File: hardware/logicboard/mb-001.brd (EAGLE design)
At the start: 91 x 57 mm, 11 parts, among them J7 DIN5, J8 DIN5, J9 DIN5

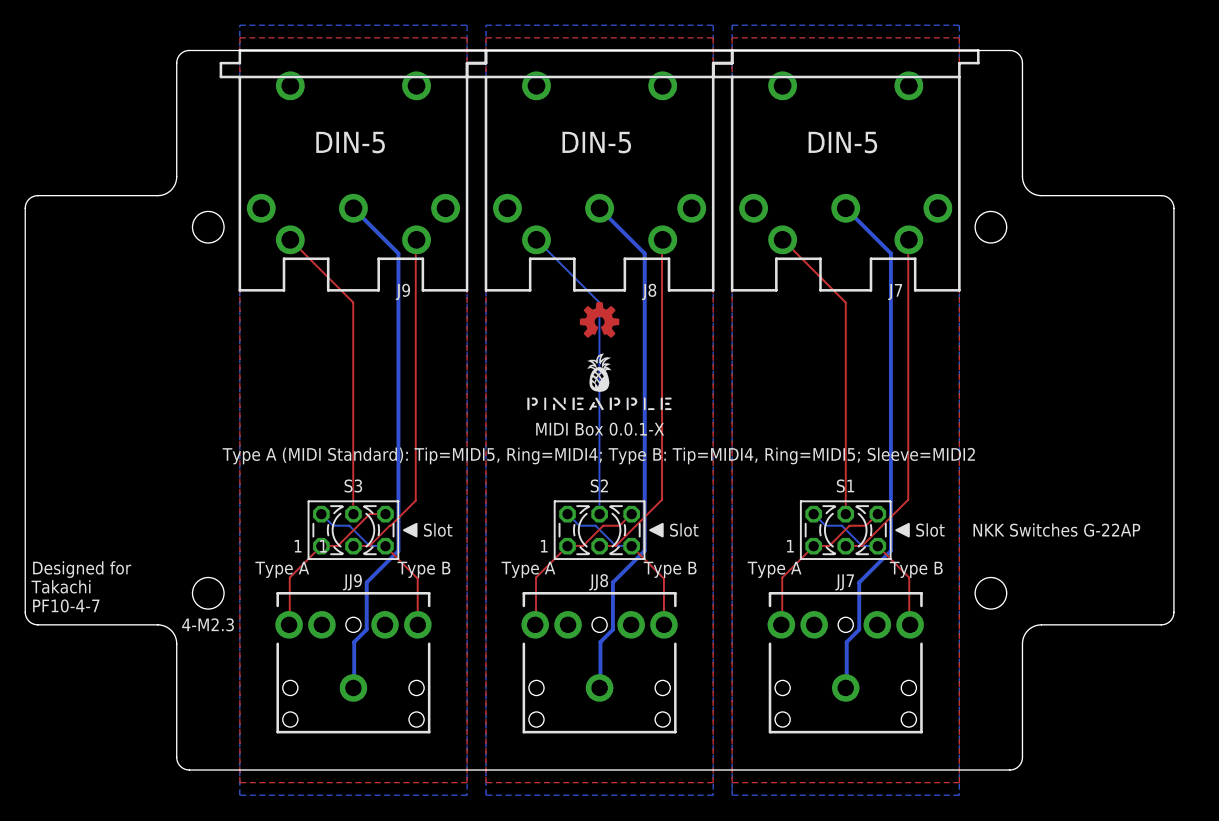
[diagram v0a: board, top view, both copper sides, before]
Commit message: Fixed silk and signal names. No pattern changed.
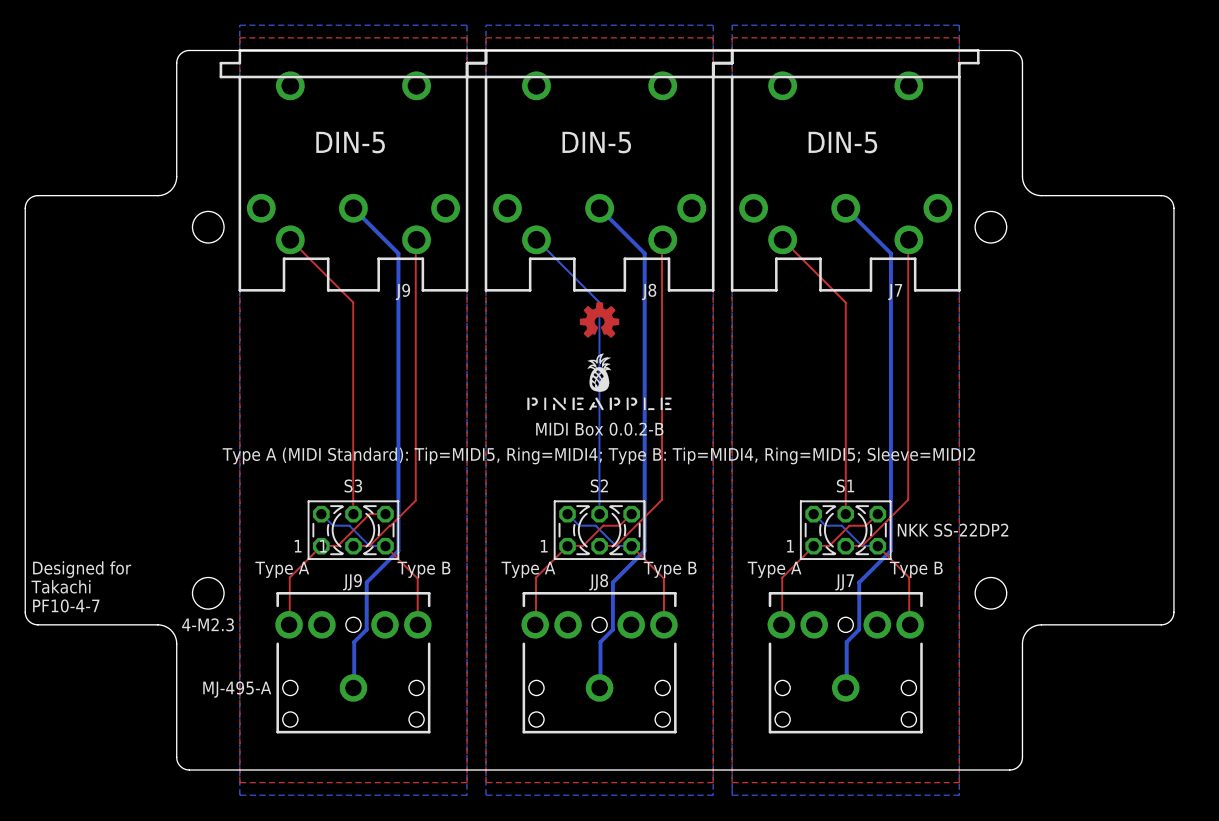
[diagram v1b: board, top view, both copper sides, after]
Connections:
- removed net M1RNG: JJ7.RING, S1.1, S1.6
- removed net M2RNG: JJ8.RING, S2.1, S2.6
- removed net M3RNG: JJ9.RING, S3.1, S3.6
- new net M1RING: JJ7.TIP, S1.3, S1.4
- new net M2RING: JJ8.TIP, S2.3, S2.4
- new net M3RING: JJ9.TIP, S3.3, S3.4
- net M1TIP: now also JJ7.RING, S1.1, S1.6; no longer JJ7.TIP, S1.3, S1.4
- net M2TIP: now also JJ8.RING, S2.1, S2.6; no longer JJ8.TIP, S2.3, S2.4
- net M3TIP: now also JJ9.RING, S3.1, S3.6; no longer JJ9.TIP, S3.3, S3.4
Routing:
- net M3RNG: track 13.5 -> 0.00 mm
- net M2RNG: track 13.5 -> 0.00 mm
- net M1RING: track 0.00 -> 13.5 mm
- net M1RNG: track 13.5 -> 0.00 mm
- net M2RING: track 0.00 -> 13.4 mm
- net M3RING: track 0.00 -> 13.4 mm
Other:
- board text added: "MIDI Box 0.0.2-B"
- board text added: "MJ-495-A"
- board text added: "NKK SS-22DP2"
- board text removed: "MIDI Box 0.0.1-X"
- board text removed: "NKK Switches G-22AP"
- board text removed: "Slot"
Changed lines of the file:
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@@
 <rectangle x1="12" y1="0" x2="79" y2="1" layer="42"/>
 <rectangle x1="0" y1="11.5" x2="1" y2="45.5" layer="42"/>
-<text x="45.5" y="27" size="1" layer="25" align="center">MIDI Box 0.0.1-X</text>
+<text x="45.5" y="27" size="1" layer="25" align="center">MIDI Box 0.0.2-B</text>
 <hole x="76.5" y="14" drill="2.5"/>
 <hole x="76.5" y="43" drill="2.5"/>
@@
 <text x="14.5" y="11.5" size="1" layer="25" align="center">4-M2.3</text>
 <text x="45.5" y="25" size="1" layer="25" align="center">Type A (MIDI Standard): Tip=MIDI5, Ring=MIDI4; Type B: Tip=MIDI4, Ring=MIDI5; Sleeve=MIDI2</text>
-<text x="70.5" y="19" size="1" layer="25" align="center-left">Slot</text>
-<polygon width="0.1524" layer="21">
-<vertex x="69" y="19"/>
-<vertex x="70" y="19.5"/>
-<vertex x="70" y="18.5"/>
-</polygon>
+<text x="69" y="19" size="1" layer="25" align="center-left">NKK SS-22DP2</text>
 <text x="68.5" y="16" size="1" layer="25" align="center-left">Type B</text>
 <text x="61.5" y="16" size="1" layer="25" align="center-right">Type A</text>
@@
 <text x="49" y="16" size="1" layer="25" align="center-left">Type B</text>
 <text x="29.5" y="16" size="1" layer="25" align="center-left">Type B</text>
-<text x="51" y="19" size="1" layer="25" align="center-left">Slot</text>
-<polygon width="0.1524" layer="21">
-<vertex x="49.5" y="19"/>
-<vertex x="50.5" y="19.5"/>
-<vertex x="50.5" y="18.5"/>
-</polygon>
-<text x="31.5" y="19" size="1" layer="25" align="center-left">Slot</text>
-<polygon width="0.1524" layer="21">
-<vertex x="30" y="19"/>
-<vertex x="31" y="19.5"/>
-<vertex x="31" y="18.5"/>
-</polygon>
 <text x="24" y="17.73" size="1" layer="25" align="center-right">1</text>
 <text x="41.5" y="17.73" size="1" layer="25" align="center-right">1</text>
@@
 <text x="48.04" y="16" size="1" layer="26" rot="MR0" align="center-right">TIP</text>
 <text x="45.5" y="4.5" size="1" layer="26" rot="MR0" align="center">SLV</text>
-<text x="40.42" y="9.5" size="1" layer="26" rot="MR0" align="center">RNG</text>
-<text x="50.58" y="9.5" size="1" layer="26" rot="MR0" align="center">TIP</text>
+<text x="40.42" y="9.5" size="1" layer="26" rot="MR0" align="center">TIP</text>
+<text x="50.58" y="9.5" size="1" layer="26" rot="MR0" align="center">RNG</text>
 <text x="45.5" y="42" size="1" layer="26" rot="MR0" align="center">GND</text>
 <text x="40.42" y="39.5" size="1" layer="26" rot="MR0" align="center">SND</text>
@@
 <text x="20.92" y="39.5" size="1" layer="26" rot="MR0" align="center">SND</text>
 <text x="31.08" y="39.5" size="1" layer="26" rot="MR0" align="center">RTN</text>
-<text x="20.92" y="9.5" size="1" layer="26" rot="MR0" align="center">RNG</text>
-<text x="31.08" y="9.5" size="1" layer="26" rot="MR0" align="center">TIP</text>
+<text x="20.92" y="9.5" size="1" layer="26" rot="MR0" align="center">TIP</text>
+<text x="31.08" y="9.5" size="1" layer="26" rot="MR0" align="center">RNG</text>
 <text x="26" y="4.5" size="1" layer="26" rot="MR0" align="center">SLV</text>
 <text x="65" y="4.5" size="1" layer="26" rot="MR0" align="center">SLV</text>
-<text x="70.08" y="9.5" size="1" layer="26" rot="MR0" align="center">TIP</text>
-<text x="59.42" y="9.5" size="1" layer="26" rot="MR0" align="center">RNG</text>
+<text x="70.08" y="9.5" size="1" layer="26" rot="MR0" align="center">RNG</text>
+<text x="59.42" y="9.5" size="1" layer="26" rot="MR0" align="center">TIP</text>
 <text x="65" y="16" size="1" layer="26" rot="MR0" align="center">RTN</text>
 <text x="65" y="22" size="1" layer="26" rot="MR0" align="center">SND</text>
@@
 <text x="28.54" y="22" size="1" layer="26" rot="MR0" align="center-right">RNG</text>
 <text x="22" y="17.73" size="1" layer="25" align="center-right">1</text>
-<text x="75" y="19" size="1" layer="25" align="center-left">NKK Switches G-22AP</text>
+<text x="19.5" y="6.5" size="1" layer="25" align="center-right">MJ-495-A</text>
 </plain>
 <attributes>
@@
 <wire x1="60.0456" y1="41.9862" x2="60" y2="42" width="0.1524" layer="1"/>
 </signal>
-<signal name="M1TIP">
+<signal name="M1RING">
 <contactref element="S1" pad="3"/>
 <contactref element="JJ7" pad="TIP"/>
@@
 <wire x1="67.5894" y1="17.6784" x2="67.54" y2="17.73" width="0.1524" layer="1"/>
 </signal>
-<signal name="M1RNG">
+<signal name="M1TIP">
 <contactref element="JJ7" pad="RING"/>
 <contactref element="S1" pad="6"/>
@@
 <wire x1="40.5384" y1="41.9862" x2="40.5" y2="42" width="0.1524" layer="16"/>
 </signal>
-<signal name="M2TIP">
+<signal name="M2RING">
 <contactref element="S2" pad="3"/>
 <contactref element="JJ8" pad="TIP"/>
@@
 <wire x1="48.0822" y1="17.6784" x2="48.04" y2="17.73" width="0.1524" layer="1"/>
 </signal>
-<signal name="M2RNG">
+<signal name="M2TIP">
 <contactref element="S2" pad="1"/>
 <contactref element="JJ8" pad="RING"/>
@@
 <wire x1="21.0312" y1="41.9862" x2="21" y2="42" width="0.1524" layer="1"/>
 </signal>
-<signal name="M3TIP">
+<signal name="M3RING">
 <contactref element="S3" pad="3"/>
 <contactref element="JJ9" pad="TIP"/>
@@
 <wire x1="28.575" y1="17.6784" x2="28.54" y2="17.73" width="0.1524" layer="1"/>
 </signal>
-<signal name="M3RNG">
+<signal name="M3TIP">
 <contactref element="S3" pad="1"/>
 <contactref element="S3" pad="6"/>
